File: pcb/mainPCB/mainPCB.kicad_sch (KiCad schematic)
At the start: 0 parts

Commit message: wip pccb
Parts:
- added U1: ESP32-S3-DevKitC, PCM_Espressif:ESP32-S3-DevKitC, symbol PCM_Espressif:ESP32-S3-DevKitC
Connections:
- new net: U1.1 (3V3), U1.2 (3V3)
- new net: U1.22 (GND), U1.23 (GND), U1.24 (GND), U1.44 (GND)
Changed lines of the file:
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@@
 	(generator_version "9.0")
 	(paper "A4")
+	(symbol
+		(lib_id "PCM_Espressif:ESP32-S3-DevKitC")
+		(at 129.54 97.79 0)
+		(unit 1)
+		(exclude_from_sim no)
+		(in_bom yes)
+		(on_board yes)
+		(dnp no)
+		(fields_autoplaced yes)
+		(property "Reference" "U1"
+			(at 131.6833 143.51 0)
+			(effects
+				(font
+					(size 1.27 1.27)
+				)
+				(justify left)
+			)
+		)
+		(property "Value" "ESP32-S3-DevKitC"
+			(at 131.6833 146.05 0)
+			(effects
+				(font
+					(size 1.27 1.27)
+				)
+				(justify left)
+			)
+		)
+		(property "Footprint" "PCM_Espressif:ESP32-S3-DevKitC"
+			(at 129.54 154.94 0)
+			(effects
+				(font
+					(size 1.27 1.27)
+				)
+				(hide yes)
+			)
+		)
+		(property "Datasheet" ""
+			(at 69.85 100.33 0)
+			(effects
+				(font
+					(size 1.27 1.27)
+				)
+				(hide yes)
+			)
+		)
+		(property "Description" "ESP32-S3-DevKitC"
+			(at 129.54 97.79 0)
+			(effects
+				(font
+					(size 1.27 1.27)
+				)
+				(hide yes)
+			)
+		)
+		(pin "13"
+		)
+		(pin "7"
+		)
+		(pin "4"
+		)
+		(pin "31"
+		)
+		(pin "16"
+		)
+		(pin "11"
+		)
+		(pin "40"
+		)
+		(pin "20"
+		)
+		(pin "32"
+		)
+		(pin "35"
+		)
+		(pin "17"
+		)
+		(pin "39"
+		)
+		(pin "2"
+		)
+		(pin "24"
+		)
+		(pin "1"
+		)
+		(pin "6"
+		)
+		(pin "37"
+		)
+		(pin "15"
+		)
+		(pin "44"
+		)
+		(pin "19"
+		)
+		(pin "23"
+		)
+		(pin "34"
+		)
+		(pin "26"
+		)
+		(pin "22"
+		)
+		(pin "30"
+		)
+		(pin "8"
+		)
+		(pin "33"
+		)
+		(pin "43"
+		)
+		(pin "9"
+		)
+		(pin "36"
+		)
+		(pin "28"
+		)
+		(pin "12"
+		)
+		(pin "5"
+		)
+		(pin "41"
+		)
+		(pin "21"
+		)
+		(pin "38"
+		)
+		(pin "27"
+		)
+		(pin "18"
+		)
+		(pin "3"
+		)
+		(pin "14"
+		)
+		(pin "42"
+		)
+		(pin "29"
+		)
+		(pin "25"
+		)
+		(pin "10"
+		)
+		(instances
+			(project ""
+				(path "/27c374aa-4c81-4903-a17b-9cdb1b485207"
+					(reference "U1")
+					(unit 1)
+				)
+			)
+		)
+	)
 	(sheet_instances
 		(path "/"

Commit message: oskur, cette personne fait sûrement n'imp mais ne s'en aperçois même pas (découvrez son histoire)
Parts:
- added J1: Conn_01x30, Chris:FPC_30_Dell_0.8mm_no0, symbol Connector_Generic:Conn_01x30
- added J2: Conn_02x15_Counter_Clockwise, Connector_PinHeader_2.54mm:PinHeader_2x15_P2.54mm_Vertical, symbol Connector_Generic:Conn_02x15_Counter_Clockwise
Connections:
- net at U1.5 (GPIO5/ADC1_CH4): now also J1.14 (Pin_14), J2.14 (Pin_14)
- new net: J1.1 (Pin_1), J2.1 (Pin_1)
- new net: J1.10 (Pin_10), J2.10 (Pin_10)
- new net: J1.11 (Pin_11), J2.11 (Pin_11)
- new net: J1.12 (Pin_12), J2.12 (Pin_12)
- new net: J1.13 (Pin_13), J2.13 (Pin_13)
- new net: J1.15 (Pin_15), J2.15 (Pin_15)
- new net: J1.16 (Pin_16), J2.16 (Pin_16)
- new net: J1.17 (Pin_17), J2.17 (Pin_17)
- new net: J1.18 (Pin_18), J2.18 (Pin_18)
- new net: J1.19 (Pin_19), J2.19 (Pin_19)
- new net: J1.2 (Pin_2), J2.2 (Pin_2)
- new net: J1.20 (Pin_20), J2.20 (Pin_20)
- new net: J1.21 (Pin_21), J2.21 (Pin_21)
- new net: J1.22 (Pin_22), J2.22 (Pin_22)
- new net: J1.23 (Pin_23), J2.23 (Pin_23)
- new net: J1.24 (Pin_24), J2.24 (Pin_24)
- new net: J1.25 (Pin_25), J2.25 (Pin_25)
- new net: J1.26 (Pin_26), J2.26 (Pin_26)
- new net: J1.27 (Pin_27), J2.27 (Pin_27)
- new net: J1.28 (Pin_28), J2.28 (Pin_28)
- new net: J1.29 (Pin_29), J2.29 (Pin_29)
- new net: J1.3 (Pin_3), J2.3 (Pin_3)
- new net: J1.30 (Pin_30), J2.30 (Pin_30)
- new net: J1.4 (Pin_4), J2.4 (Pin_4)
- new net: J1.5 (Pin_5), J2.5 (Pin_5)
- new net: J1.6 (Pin_6), J2.6 (Pin_6)
- new net: J1.7 (Pin_7), J2.7 (Pin_7)
- new net: J1.8 (Pin_8), J2.8 (Pin_8)
- new net: J1.9 (Pin_9), J2.9 (Pin_9)

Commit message: pcb: hmmm yes that's better with labels
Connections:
- net GND: now reaches J1.1 (Pin_1), J2.1 (Pin_1)
- net GND: now also U1.22 (GND), U1.23 (GND), U1.24 (GND), U1.44 (GND)
- net P10: now reaches J1.10 (Pin_10), J2.10 (Pin_10)
- net P11: now reaches J1.11 (Pin_11), J2.11 (Pin_11)
- net P12: now reaches J1.12 (Pin_12), J2.12 (Pin_12)
- net P13: now reaches J1.13 (Pin_13), J2.13 (Pin_13)
- net P14: now reaches J1.14 (Pin_14), J2.14 (Pin_14)
- net P14: no longer U1.5 (GPIO5/ADC1_CH4)
- net P15: now reaches J1.15 (Pin_15), J2.15 (Pin_15)
- net P16: now reaches J1.16 (Pin_16), J2.16 (Pin_16)
- net P17: now reaches J1.17 (Pin_17), J2.17 (Pin_17)
- net P18: now reaches J1.18 (Pin_18), J2.18 (Pin_18)
- net P19: now reaches J1.19 (Pin_19), J2.19 (Pin_19)
- net P02: now reaches J1.2 (Pin_2), J2.2 (Pin_2)
- net P20: now reaches J1.20 (Pin_20), J2.20 (Pin_20)
- net P21: now reaches J1.21 (Pin_21), J2.21 (Pin_21)
- net P22: now reaches J1.22 (Pin_22), J2.22 (Pin_22)
- net P23: now reaches J1.23 (Pin_23), J2.23 (Pin_23)
- net P24: now reaches J1.24 (Pin_24), J2.24 (Pin_24)
- net P25: now reaches J1.25 (Pin_25), J2.25 (Pin_25)
- net P26: now reaches J1.26 (Pin_26), J2.26 (Pin_26)
- net P27: now reaches J1.27 (Pin_27), J2.27 (Pin_27)
- net P28: now reaches J1.28 (Pin_28), J2.28 (Pin_28)
- net P29: now reaches J1.29 (Pin_29), J2.29 (Pin_29)
- net P03: now reaches J1.3 (Pin_3), J2.3 (Pin_3)
- net P30: now reaches J1.30 (Pin_30), J2.30 (Pin_30)
- net P04: now reaches J1.4 (Pin_4), J2.4 (Pin_4)
- net P05: now reaches J1.5 (Pin_5), J2.5 (Pin_5)
- net P06: now reaches J1.6 (Pin_6), J2.6 (Pin_6)
- net P07: now reaches J1.7 (Pin_7), J2.7 (Pin_7)
- net P08: now reaches J1.8 (Pin_8), J2.8 (Pin_8)
- net P09: now reaches J1.9 (Pin_9), J2.9 (Pin_9)

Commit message: wip: starting pcb wiring
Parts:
- added R1: 220, Resistor_THT:R_Axial_DIN0207_L6.3mm_D2.5mm_P10.16mm_Horizontal, symbol Device:R
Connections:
- net at U1.27 (GPIO21): now also R1.2
- net P02 renamed P02_unused
- net P03 renamed P03_unused
- net P04 renamed P04_CAP_LED
- net P04_CAP_LED: now also R1.1
- net P05 renamed P05_O10
- net P06 renamed P06_O11
- net P07 renamed P07_O9
- net P08 renamed P08_O14
- net P09 renamed P09_O13
- net P10 renamed P10_O15
- net P11 renamed P11_O16
- net P12 renamed P12_O12
- net P13 renamed P13_O0
- net P14 renamed P14_O2
- net P15 renamed P15_O1
- net P16 renamed P16_O3
- net P17 renamed P17_O8
- net P18 renamed P18_O6
- net P19 renamed P19_O7
- net P20 renamed P20_O4
- net P21 renamed P21_O5
- net P22 renamed P22_I0
- net P23 renamed P23_I3
- net P24 renamed P24_I1
- net P25 renamed P25_I5
- net P26 renamed P26_I2
- net P27 renamed P27_I4
- net P28 renamed P28_I6
- net P29 renamed P29_I7
- net P30 renamed P30_unused_kb_det

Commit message: wip: starting no crossing cable
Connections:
- net P22_I0: now also U1.38 (GPIO41/MTDI)
- net P24_I1: now also U1.39 (GPIO42/MTMS)
- net P26_I2: now also U1.40 (GPIO2/ADC1_CH1)
- net P28_I6: now also U1.41 (GPIO1/ADC1_CH0)
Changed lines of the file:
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@@
+		)
+	)
+	(global_label "P28_I6"
+		(shape input)
+		(at 154.94 77.47 0)
+		(fields_autoplaced yes)
+		(effects
+			(font
+				(size 1.27 1.27)
+			)
+			(justify left)
+		)
+		(property "Intersheetrefs" "${INTERSHEET_REFS}"
+			(at 164.3961 77.47 0)
+			(effects
+				(font
+					(size 1.27 1.27)
+				)
+				(justify left)
+				(hide yes)
+			)
 		)
 	)
@@
 		)
 	)
+	(global_label "P26_I2"
+		(shape input)
+		(at 154.94 80.01 0)
+		(fields_autoplaced yes)
+		(effects
+			(font
+				(size 1.27 1.27)
+			)
+			(justify left)
+		)
+		(property "Intersheetrefs" "${INTERSHEET_REFS}"
+			(at 164.3961 80.01 0)
+			(effects
+				(font
+					(size 1.27 1.27)
+				)
+				(justify left)
+				(hide yes)
+			)
+		)
+	)
 	(global_label "P07_O9"
 		(shape input)
@@
 	(global_label "P22_I0"
 		(shape input)
+		(at 104.14 80.01 180)
+		(fields_autoplaced yes)
+		(effects
+			(font
+				(size 1.27 1.27)
+			)
+			(justify right)
+		)
+		(property "Intersheetrefs" "${INTERSHEET_REFS}"
+			(at 94.6839 80.01 0)
+			(effects
+				(font
+					(size 1.27 1.27)
+				)
+				(justify right)
+				(hide yes)
+			)
+		)
+	)
+	(global_label "P22_I0"
+		(shape input)
 		(at 212.09 111.76 180)
 		(fields_autoplaced yes)
@@
 				(hide yes)
 			)
+		)
+	)
+	(global_label "P24_I1"
+		(shape input)
+		(at 104.14 82.55 180)
+		(fields_autoplaced yes)
+		(effects
+			(font
+				(size 1.27 1.27)
+			)
+			(justify right)
+		)
+		(property "Intersheetrefs" "${INTERSHEET_REFS}"
+			(at 94.6839 82.55 0)
+			(effects
+				(font
+					(size 1.27 1.27)
+				)
+				(justify right)
+				(hide yes)
+			)

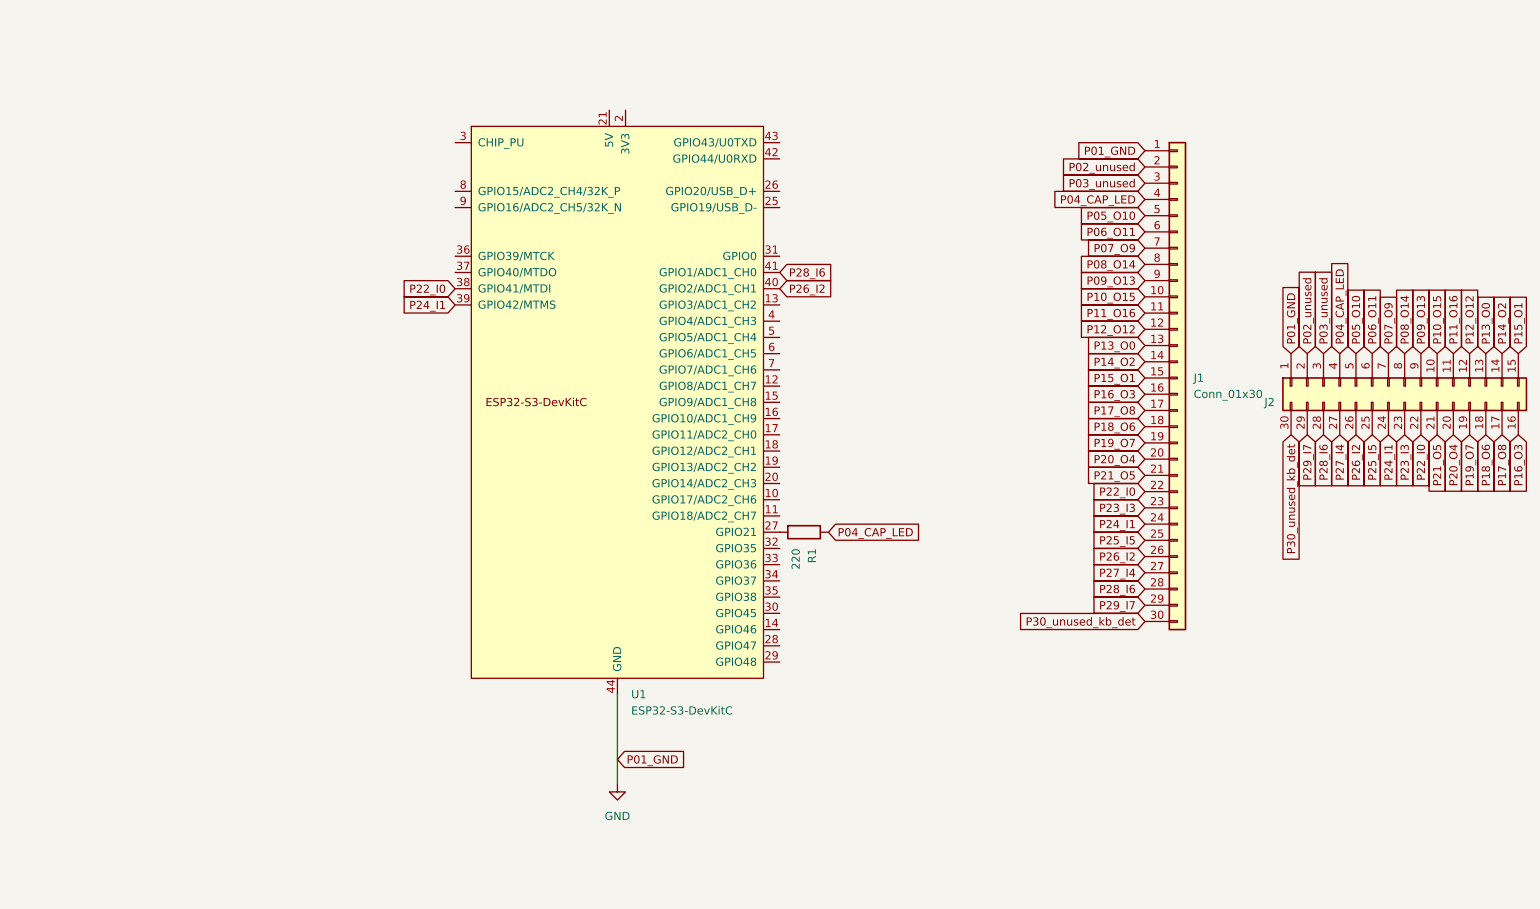
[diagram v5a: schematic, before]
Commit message: chore: adding backlight connectors
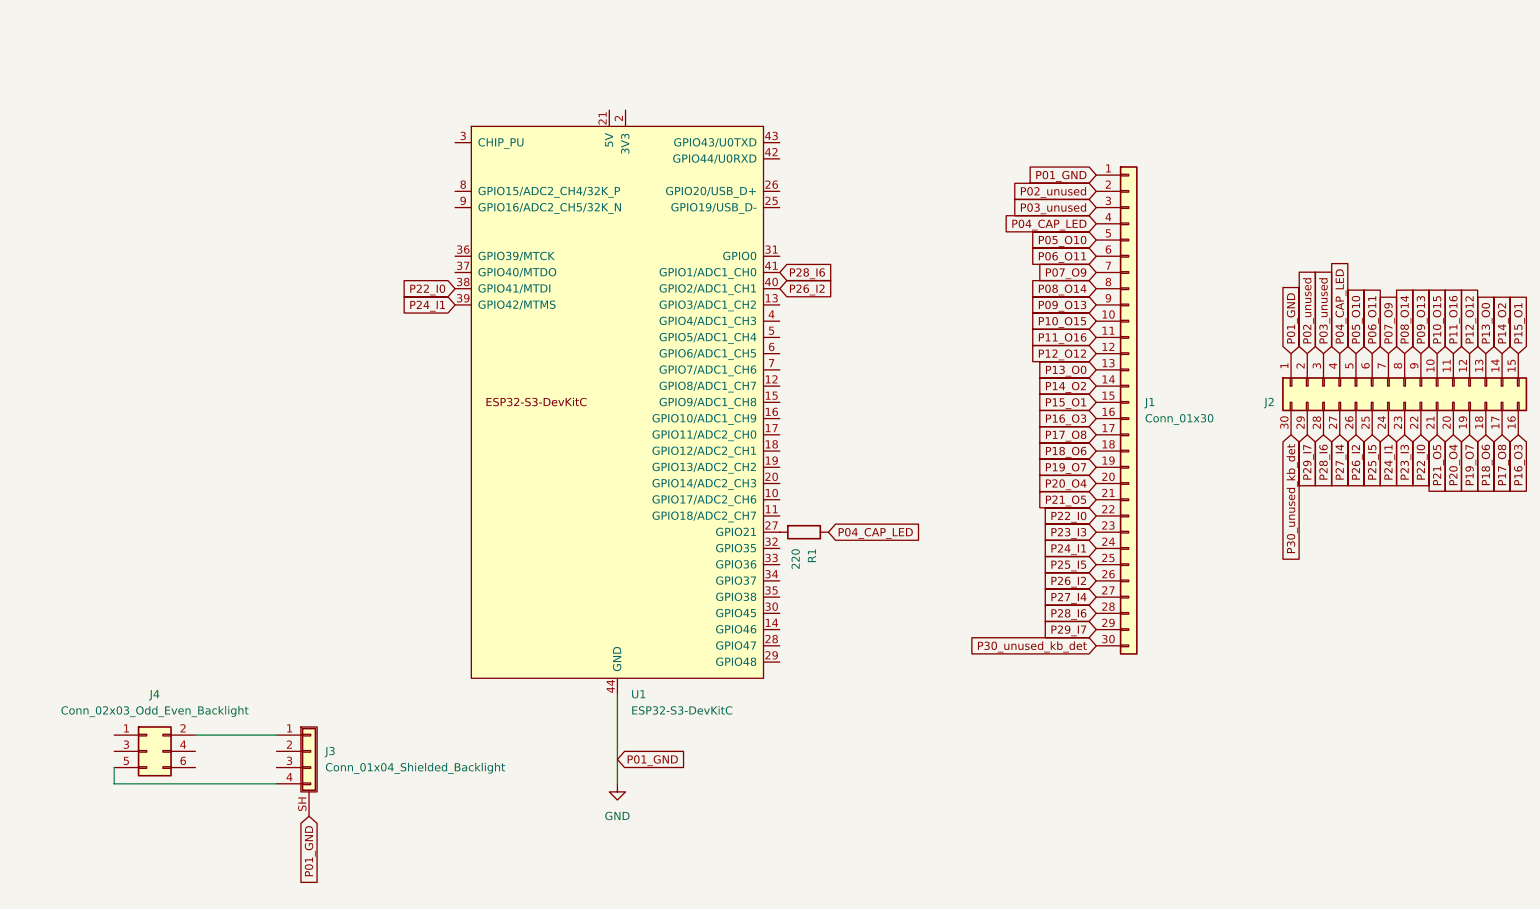
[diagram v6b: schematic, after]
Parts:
- added J3: Conn_01x04_Shielded_Backlight, Chris:FPC_4_Dell_1mm_with0, symbol Connector_Generic_Shielded:Conn_01x04_Shielded
- added J4: Conn_02x03_Odd_Even_Backlight, Connector_PinHeader_2.00mm:PinHeader_2x03_P2.00mm_Vertical, symbol Connector_Generic:Conn_02x03_Odd_Even
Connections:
- net GND: now also J3.SH (Shield)
- new net: J3.1 (Pin_1), J4.2 (Pin_2)
- new net: J3.4 (Pin_4), J4.5 (Pin_5)
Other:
- moved on the sheet: J1

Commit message: feat: adding NPN for caps led
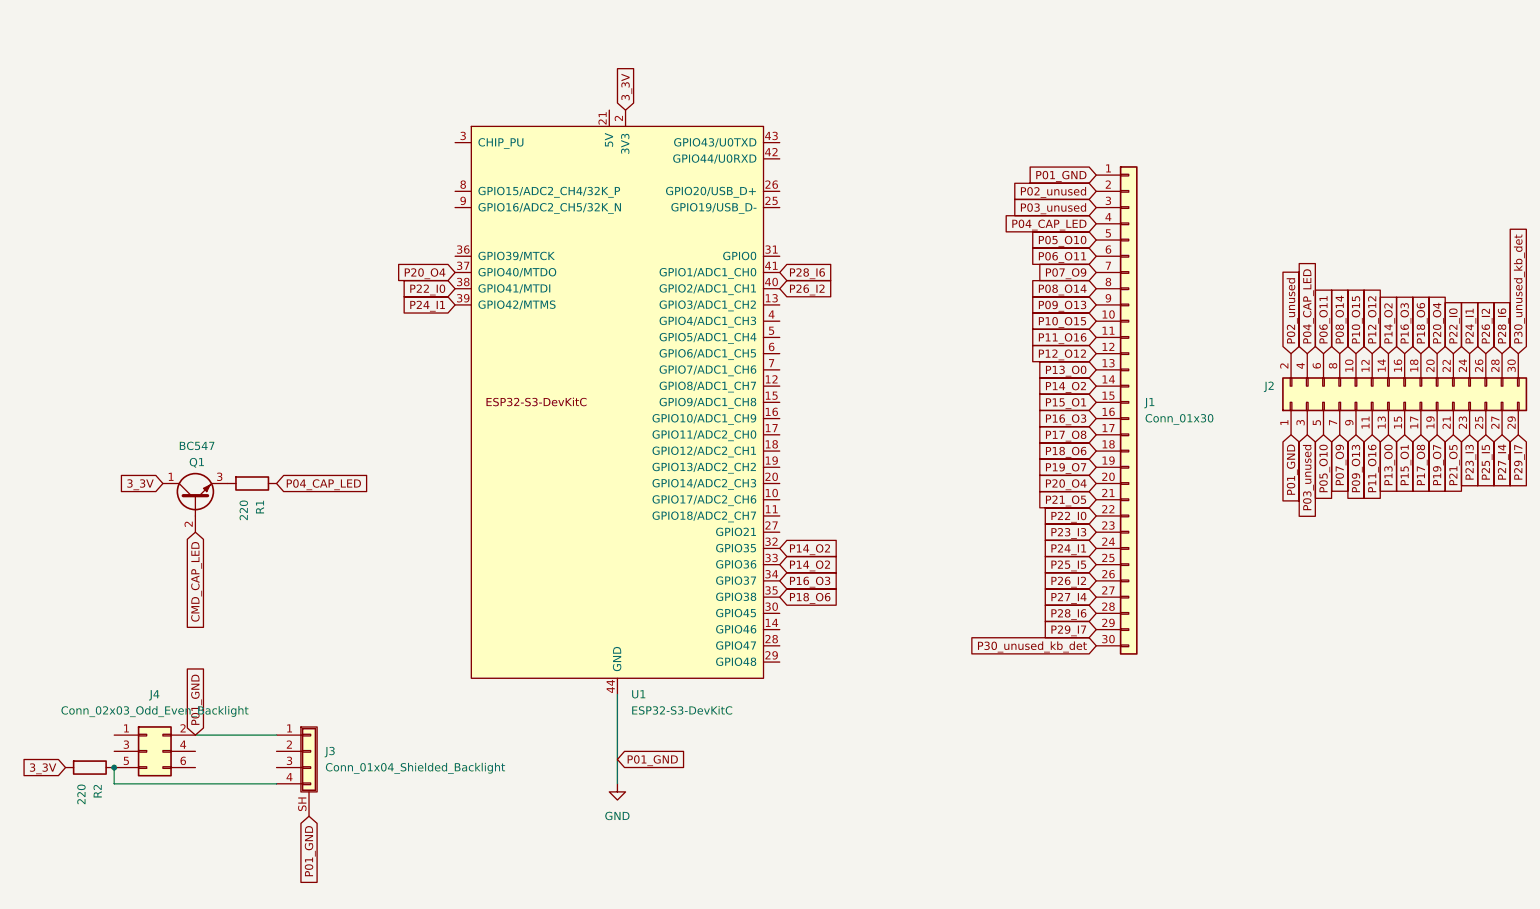
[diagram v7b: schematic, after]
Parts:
- added Q1: BC547, Package_TO_SOT_THT:TO-92_Inline, symbol Transistor_BJT:BC547
- added R2: 220, Resistor_THT:R_Axial_DIN0207_L6.3mm_D2.5mm_P10.16mm_Horizontal, symbol Device:R
- J2: symbol Connector_Generic:Conn_02x15_Counter_Clockwise -> Connector_Generic:Conn_02x15_Odd_Even
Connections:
- net GND: now also J3.1 (Pin_1), J4.2 (Pin_2)
- net P14_O2: now also U1.32 (GPIO35), U1.33 (GPIO36)
- net P16_O3: now also U1.34 (GPIO37)
- net P18_O6: now also U1.35 (GPIO38)
- net P20_O4: now also U1.37 (GPIO40/MTDO)
- net at J3.4 (Pin_4), J4.5 (Pin_5): now also R2.1
- net 3_3V: now reaches U1.1 (3V3), U1.2 (3V3)
- net 3_3V: now also Q1.1 (C), R2.2
- net at R1.2: now also Q1.3 (E); no longer U1.27 (GPIO21)
- new net CMD_CAP_LED: Q1.2 (B)
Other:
- moved on the sheet: R1

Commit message: chore: more cables
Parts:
- J1: value Conn_01x30 -> Conn_01x30_Keyboard
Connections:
- net CMD_CAP_LED: now also U1.4 (GPIO4/ADC1_CH3)
- net P05_O10: now also U1.5 (GPIO5/ADC1_CH4)
- net P07_O9: now also U1.6 (GPIO6/ADC1_CH5)
- net P09_O13: now also U1.7 (GPIO7/ADC1_CH6), U1.8 (GPIO15/ADC2_CH4/32K_P)
- net P11_O16: now also U1.9 (GPIO16/ADC2_CH5/32K_N)
- net P13_O0: now also U1.10 (GPIO17/ADC2_CH6)
- net P15_O1: now also U1.11 (GPIO18/ADC2_CH7)
- net P17_O8: now also U1.12 (GPIO8/ADC1_CH7)
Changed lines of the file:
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@@
+		)
+	)
+	(global_label "P11_O16"
+		(shape input)
+		(at 104.14 67.31 180)
+		(fields_autoplaced yes)
+		(effects
+			(font
+				(size 1.27 1.27)
+			)
+			(justify right)
+		)
+		(property "Intersheetrefs" "${INTERSHEET_REFS}"
+			(at 92.7487 67.31 0)
+			(effects
+				(font
+					(size 1.27 1.27)
+				)
+				(justify right)
+				(hide yes)
+			)
 		)
 	)
@@
 		)
 	)
+	(global_label "CMD_CAP_LED"
+		(shape input)
+		(at 154.94 85.09 0)
+		(fields_autoplaced yes)
+		(effects
+			(font
+				(size 1.27 1.27)
+			)
+			(justify left)
+		)
+		(property "Intersheetrefs" "${INTERSHEET_REFS}"
+			(at 170.9275 85.09 0)
+			(effects
+				(font
+					(size 1.27 1.27)
+				)
+				(justify left)
+				(hide yes)
+			)
+		)
+	)
 	(global_label "P02_unused"
 		(shape input)
@@
 	(global_label "P07_O9"
 		(shape input)
+		(at 154.94 90.17 0)
+		(fields_autoplaced yes)
+		(effects
+			(font
+				(size 1.27 1.27)
+			)
+			(justify left)
+		)
+		(property "Intersheetrefs" "${INTERSHEET_REFS}"
+			(at 165.1218 90.17 0)
+			(effects
+				(font
+					(size 1.27 1.27)
+				)
+				(justify left)
+				(hide yes)
+			)
+		)
+	)
+	(global_label "P07_O9"
+		(shape input)
 		(at 242.57 102.87 270)
 		(fields_autoplaced yes)
@@
 		)
 	)
+	(global_label "P13_O0"
+		(shape input)
+		(at 154.94 113.03 0)
+		(fields_autoplaced yes)
+		(effects
+			(font
+				(size 1.27 1.27)
+			)
+			(justify left)
+		)
+		(property "Intersheetrefs" "${INTERSHEET_REFS}"
+			(at 165.1218 113.03 0)
+			(effects
+				(font
+					(size 1.27 1.27)
+				)
+				(justify left)
+				(hide yes)
+			)
+		)
+	)
+	(global_label "P09_O13"
+		(shape input)
+		(at 104.14 64.77 180)
+		(fields_autoplaced yes)
+		(effects
+			(font
+				(size 1.27 1.27)
+			)
+			(justify right)
+		)
+		(property "Intersheetrefs" "${INTERSHEET_REFS}"
+			(at 92.7487 64.77 0)
+			(effects
+				(font
+					(size 1.27 1.27)
+				)
+				(justify right)
+				(hide yes)
+			)
+		)
+	)
 	(global_label "P26_I2"
 		(shape input)
@@
 		)
 	)
+	(global_label "P15_O1"
+		(shape input)
+		(at 154.94 115.57 0)
+		(fields_autoplaced yes)
+		(effects
+			(font
+				(size 1.27 1.27)
+			)
+			(justify left)
+		)
+		(property "Intersheetrefs" "${INTERSHEET_REFS}"
+			(at 165.1218 115.57 0)
+			(effects
+				(font
+					(size 1.27 1.27)
+				)
+				(justify left)
+				(hide yes)
+			)
+		)
+	)
 	(global_label "P09_O13"
 		(shape input)
@@
 		)
 	)
+	(global_label "P17_O8"
+		(shape input)
+		(at 154.94 95.25 0)
+		(fields_autoplaced yes)
+		(effects
+			(font
+				(size 1.27 1.27)
+			)
+			(justify left)
+		)
+		(property "Intersheetrefs" "${INTERSHEET_REFS}"
+			(at 165.1218 95.25 0)
+			(effects
+				(font
+					(size 1.27 1.27)
+				)
+				(justify left)
+				(hide yes)
+			)
+		)
+	)
+	(global_label "P05_O10"
+		(shape input)
+		(at 154.94 87.63 0)
+		(fields_autoplaced yes)
+		(effects
+			(font
+				(size 1.27 1.27)
+			)
+			(justify left)
+		)
+		(property "Intersheetrefs" "${INTERSHEET_REFS}"
+			(at 166.3313 87.63 0)
+			(effects
+				(font
+					(size 1.27 1.27)
+				)
+				(justify left)
+				(hide yes)
+			)
+		)
+	)
 	(global_label "P01_GND"
 		(shape input)
@@
 				)
 				(justify right)
+				(hide yes)
+			)
+		)
+	)
+	(global_label "P09_O13"
+		(shape input)
+		(at 154.94 92.71 0)
+		(fields_autoplaced yes)
+		(effects
+			(font
+				(size 1.27 1.27)
+			)
+			(justify left)
+		)
+		(property "Intersheetrefs" "${INTERSHEET_REFS}"
+			(at 166.3313 92.71 0)
+			(effects
+				(font
+					(size 1.27 1.27)
+				)
+				(justify left)
 				(hide yes)
 			)
@@
 		(on_board yes)
 		(dnp no)
-		(fields_autoplaced yes)
 		(property "Reference" "J1"
 			(at 212.09 97.7899 0)
@@
 			)
 		)
-		(property "Value" "Conn_01x30"
-			(at 212.09 100.3299 0)
-			(effects
-				(font
+		(property "Value" "Conn_01x30_Keyboard"
+			(at 194.564 139.7 0)
+			(effects
+				(font
